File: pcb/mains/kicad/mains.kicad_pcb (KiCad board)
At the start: 2 copper layers, 180 x 110 mm, 26 parts, among them J1 43160-0102, J2 43160-0103, J3 43160-0104, J4 43160-0106, J5 43650-0300, J6 43045-0200, K1 G5RL-1A-TV8 DC5, U1 IRM-45-12, U2 AP63205WU-7

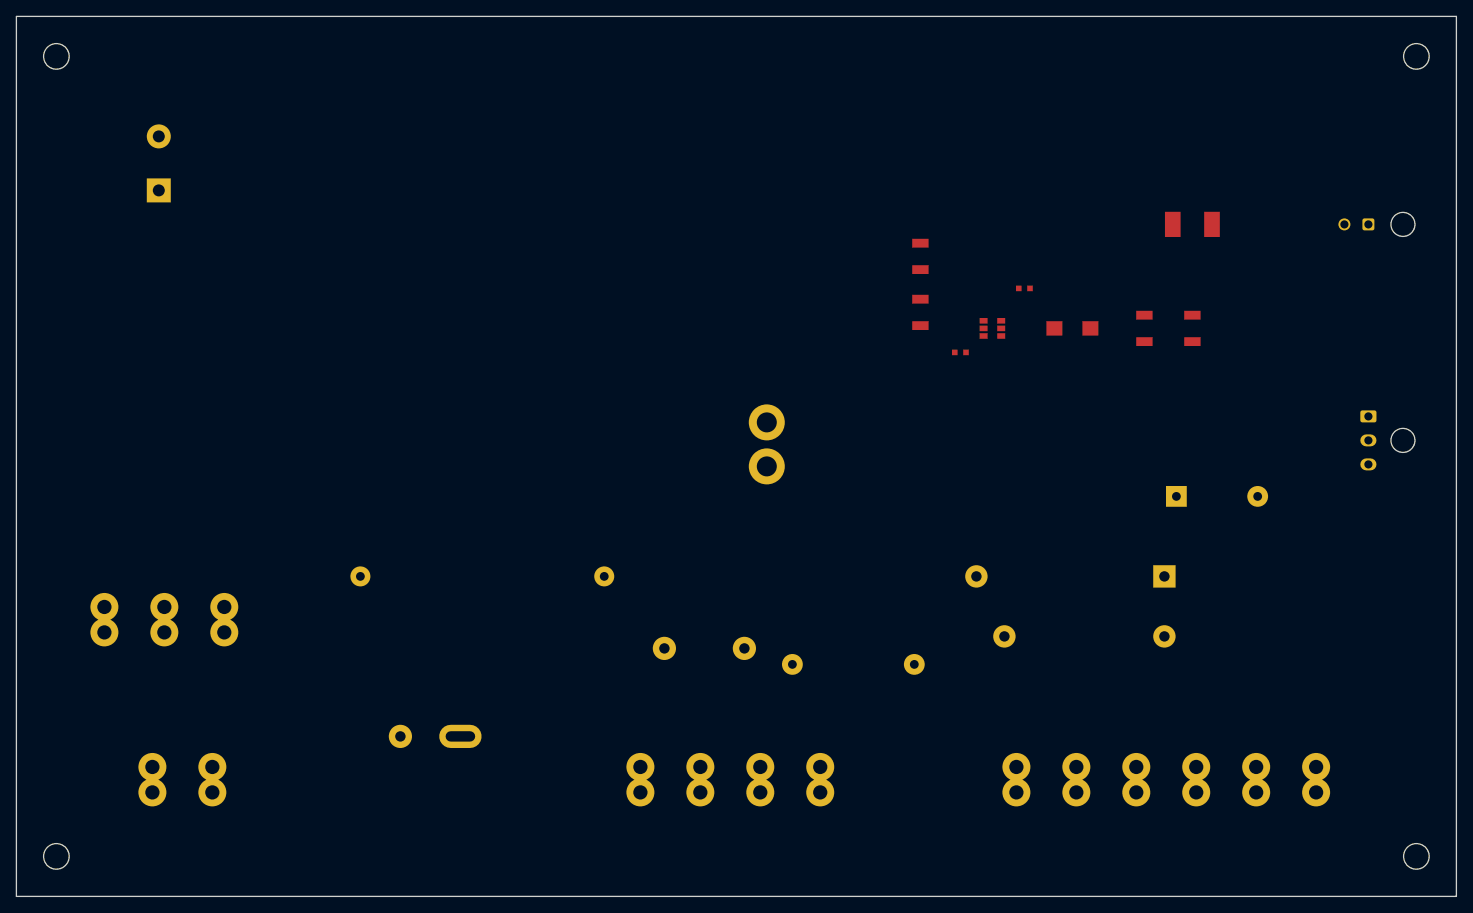
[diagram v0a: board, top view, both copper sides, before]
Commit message: Prepare filled planes and enforce KiCad routing guardrails
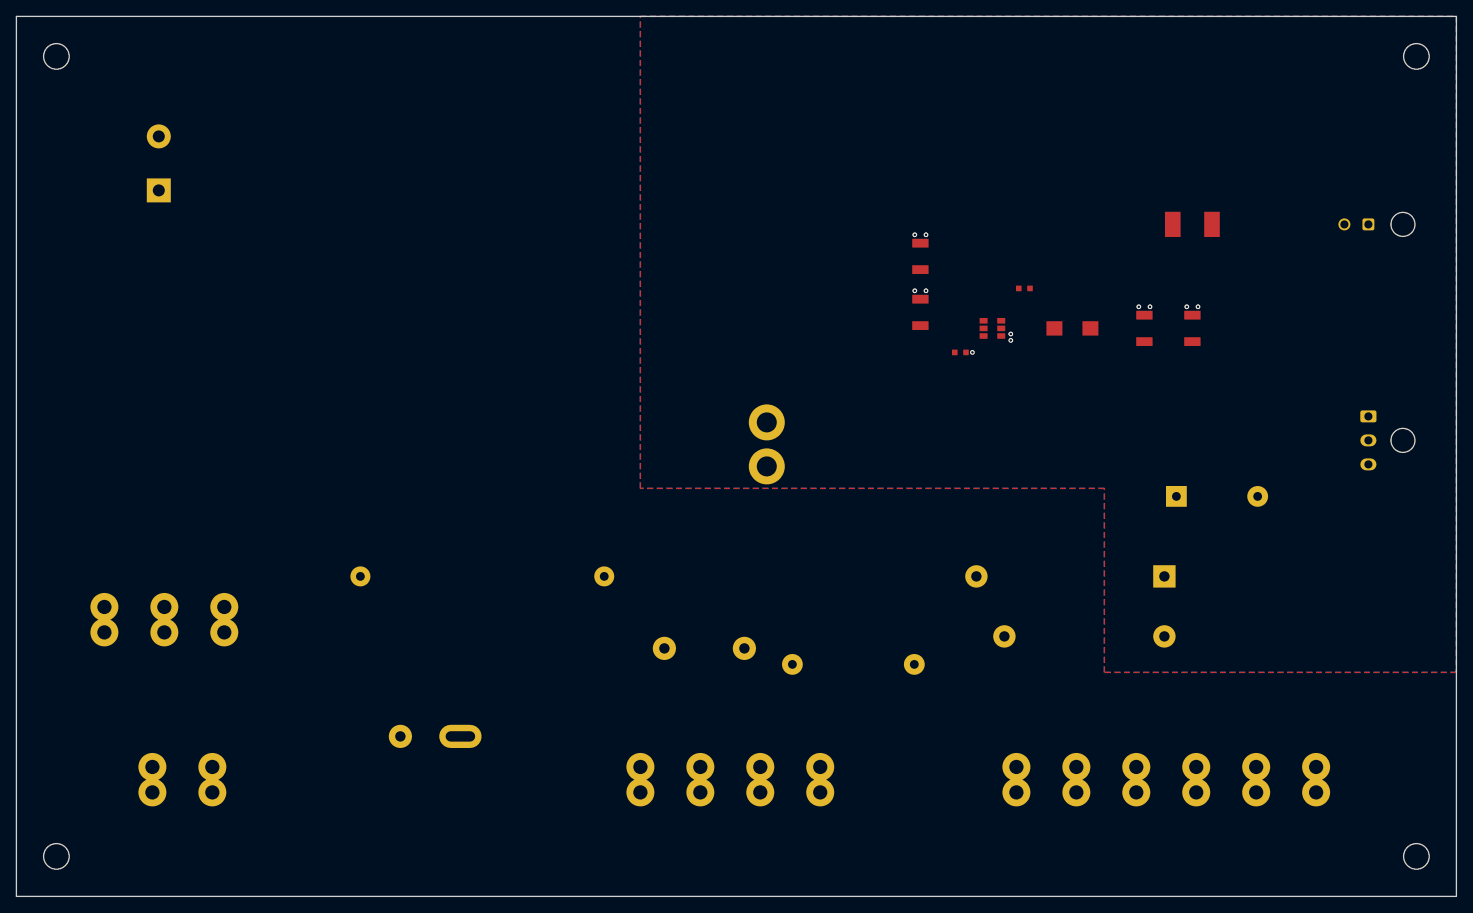
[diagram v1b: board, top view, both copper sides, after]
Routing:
- net GND_ISO: vias 0 -> 11
- added copper zone on B.Cu, net GND_ISO
- added copper zone on F.Cu, net GND_ISO

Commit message: Prepare compact three-board designs for owner routing
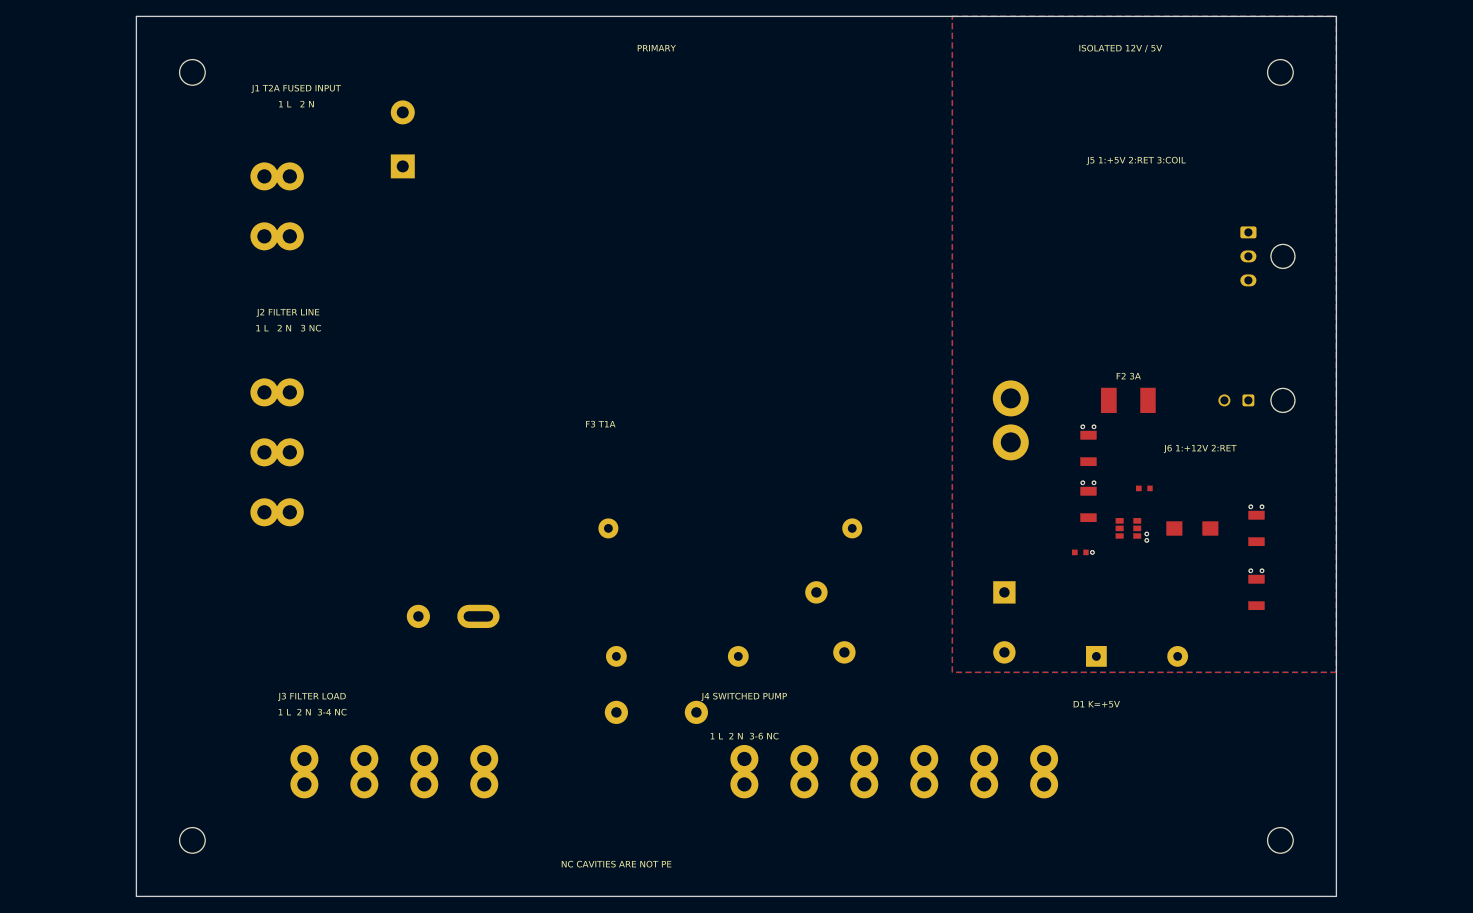
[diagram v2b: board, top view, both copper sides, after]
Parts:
- J1: value 43160-0102 -> 43160-1102
- J2: value 43160-0103 -> 43160-1103
- J3: value 43160-0104 -> 43160-1104
- J4: value 43160-0106 -> 43160-1106
- moved J1 78.3 mm to (41.0, 65.0), turned to -90 degrees
- moved J3 42.0 mm to (46.0, 141.0)
- moved J2 36.1 mm to (41.0, 92.0), turned to -90 degrees
- moved J4 34.0 mm to (101.0, 141.0)
- moved C6 34.0 mm to (165.0, 117.0)
- moved C2 31.9 mm to (144.0, 106.0)
- moved C3 31.9 mm to (144.0, 99.0)
- moved F3 31.6 mm to (84.0, 109.0)
- moved U1 30.6 mm to (53.0, 52.0)
- moved U2 30.2 mm to (149.0, 109.0)
- moved C5 29.2 mm to (151.0, 104.0)
- moved C7 29.2 mm to (143.0, 112.0)
- moved L1 29.2 mm to (157.0, 109.0)
- moved C4 28.7 mm to (165.0, 109.0)
- moved J5 27.5 mm to (164.0, 72.0)
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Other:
- board size 180 x 110 mm -> 150 x 110 mm
- board text added: "1 L 2 N"
- board text added: "1 L 2 N 3 NC"
- board text added: "1 L 2 N 3-4 NC"
- board text added: "1 L 2 N 3-6 NC"
- board text added: "D1 K=+5V"
- board text added: "F2 3A"
- board text added: "F3 T1A"
- board text added: "ISOLATED 12V / 5V"
- board text added: "J1 T2A FUSED INPUT"
- board text added: "J2 FILTER LINE"
- board text added: "J3 FILTER LOAD"
- board text added: "J4 SWITCHED PUMP"
- board text added: "J5 1:+5V 2:RET 3:COIL"
- board text added: "J6 1:+12V 2:RET"
- board text added: "NC CAVITIES ARE NOT PE"
- board text added: "PRIMARY"

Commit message: Simplify mains connectors and separate the 5 V service input
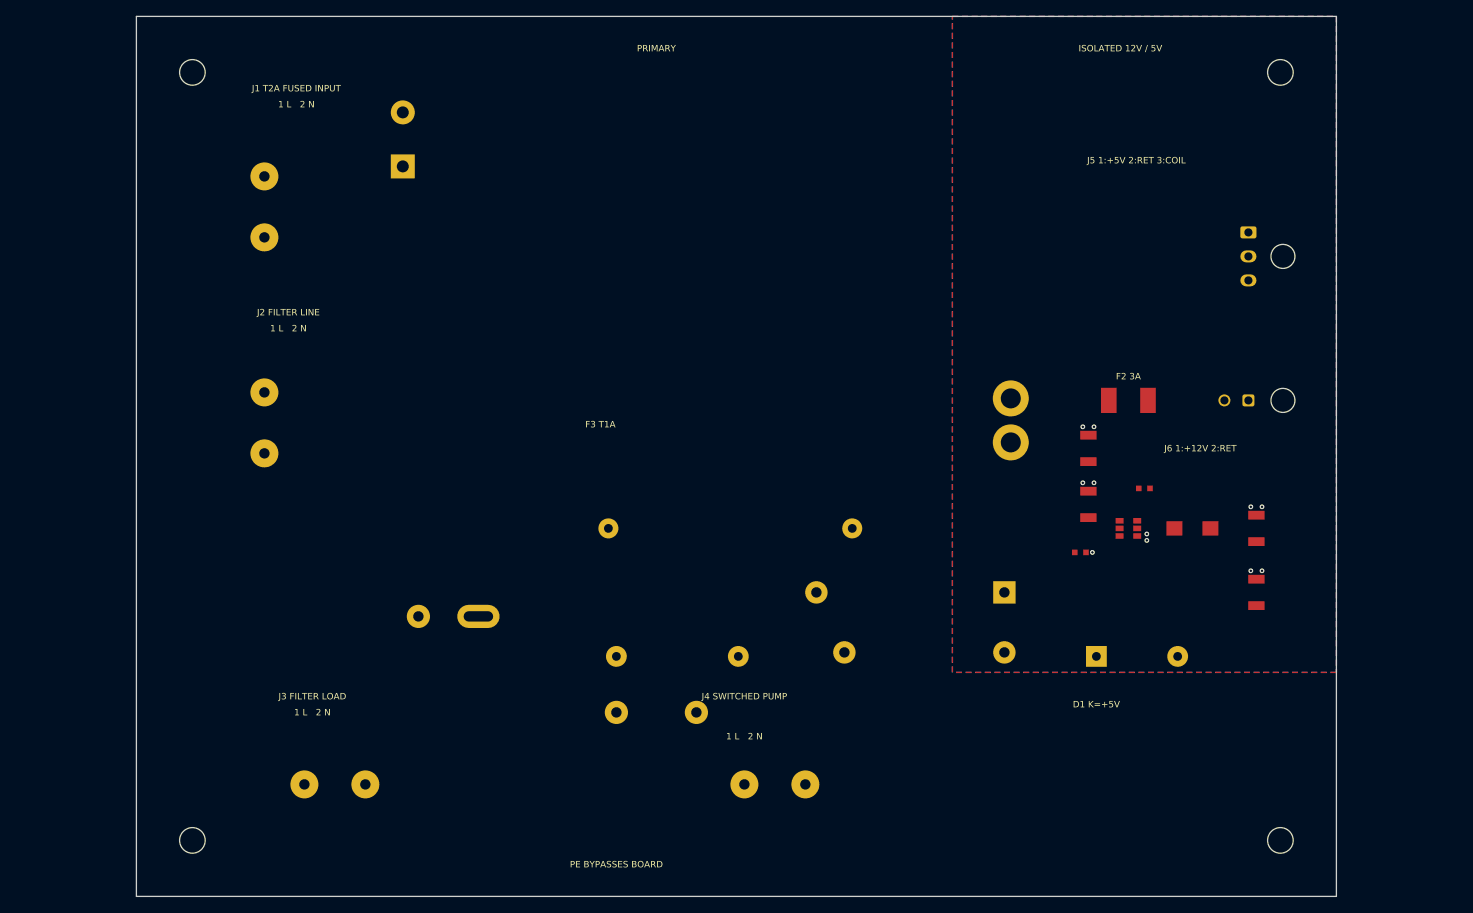
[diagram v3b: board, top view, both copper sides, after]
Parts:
- J1: value 43160-1102 -> 1868076
- J2: value 43160-1103 -> 1868076
- J3: value 43160-1104 -> 1868076
- J4: value 43160-1106 -> 1868076
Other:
- board text added: "PE BYPASSES BOARD"
- board text removed: "1 L 2 N 3 NC"
- board text removed: "1 L 2 N 3-4 NC"
- board text removed: "1 L 2 N 3-6 NC"
- board text removed: "NC CAVITIES ARE NOT PE"

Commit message: Accept completed mains routing with bounded feedback branch
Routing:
- net AC_L_FUSED: track 0.00 -> 120.7 mm
- net V5_PSU: track 0.00 -> 117.9 mm
- net AC_N: track 0.00 -> 92.6 mm
- net FILTER_LINE_L: track 0.00 -> 80.5 mm
- net COIL_DRAIN: track 0.00 -> 80.4 mm
- net PUMP_L_FILTERED: track 0.00 -> 74.4 mm
- net PUMP_N_FILTERED: track 0.00 -> 63.9 mm
- net PUMP_L_SW: track 0.00 -> 52.4 mm
- net V12_RAW: track 0.00 -> 31.0 mm
- net SNUBBER_RC: track 0.00 -> 18.1 mm
- net V12_MOTOR: track 0.00 -> 14.7 mm
- net BUCK5_SW: track 0.00 -> 9.49 mm
- net BUCK5_BST: track 0.00 -> 4.13 mm
- added copper zone on F.Cu, net V12_RAW

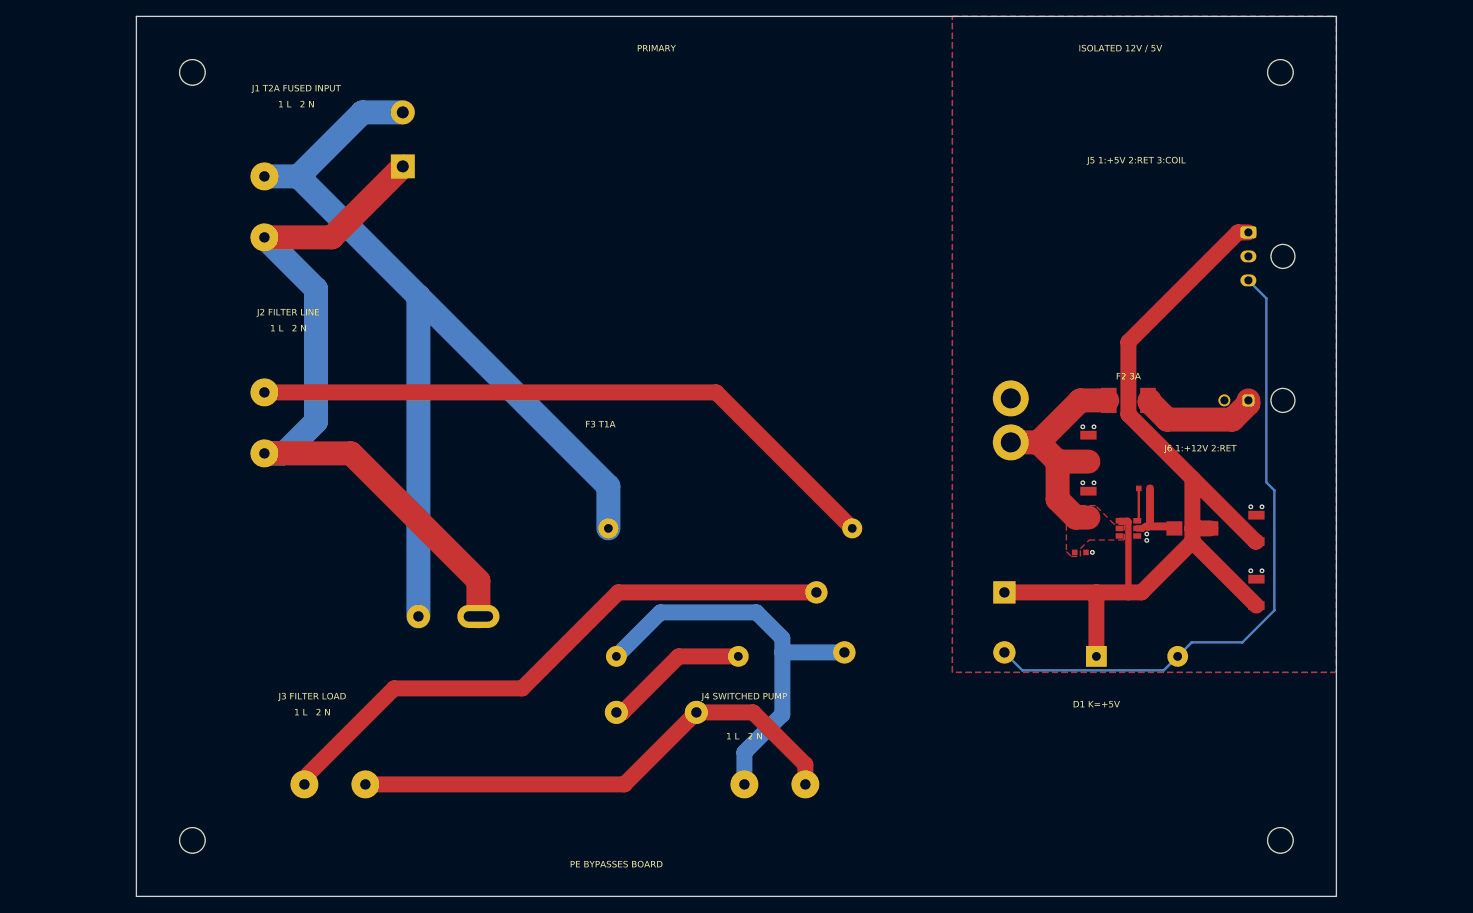
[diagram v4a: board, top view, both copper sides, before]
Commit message: Prepare all three boards for standard JLCPCB ordering
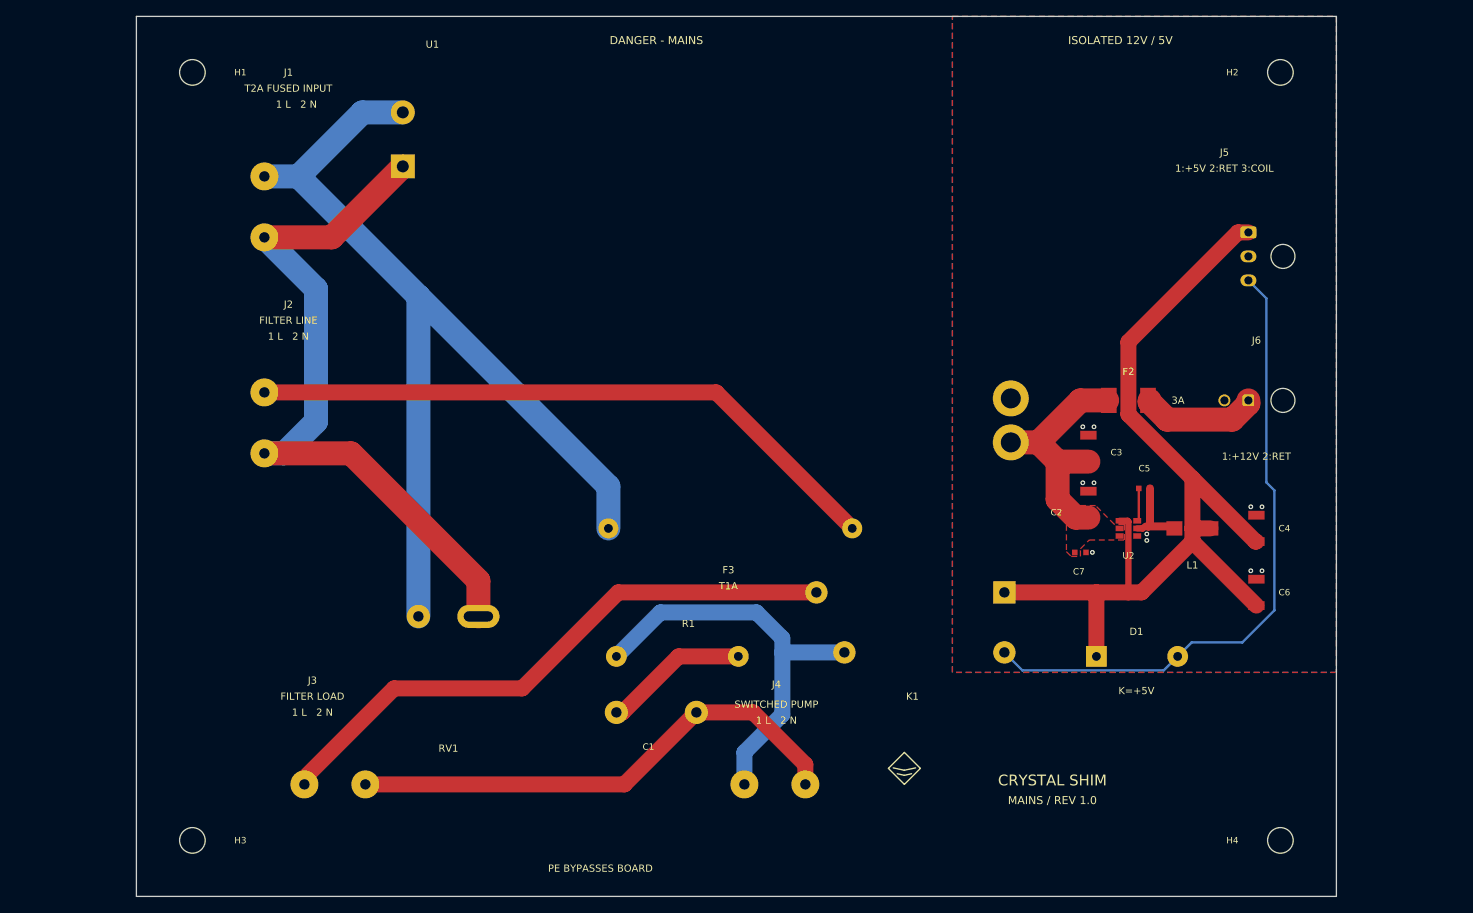
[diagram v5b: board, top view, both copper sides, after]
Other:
- board text added: "1:+12V 2:RET"
- board text added: "1:+5V 2:RET 3:COIL"
- board text added: "3A"
- board text added: "CRYSTAL SHIM"
- board text added: "DANGER - MAINS"
- board text added: "FILTER LINE"
- board text added: "FILTER LOAD"
- board text added: "K=+5V"
- board text added: "MAINS / REV 1.0"
- board text added: "SWITCHED PUMP"
- board text added: "T1A"
- board text added: "T2A FUSED INPUT"
- board text removed: "D1 K=+5V"
- board text removed: "F2 3A"
- board text removed: "F3 T1A"
- board text removed: "J1 T2A FUSED INPUT"
- board text removed: "J2 FILTER LINE"
- board text removed: "J3 FILTER LOAD"
- board text removed: "J4 SWITCHED PUMP"
- board text removed: "J5 1:+5V 2:RET 3:COIL"
- board text removed: "J6 1:+12V 2:RET"
- board text removed: "PRIMARY"
